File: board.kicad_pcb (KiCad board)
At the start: 6 copper layers, 197 x 134 mm, 6 parts, among them U1 MC68060RC50, U2 XC95144XL-5TQG100C, U3 SST39VF1601C-70-4C-EKE, U4 IS61WV51216BLL-10TLI, U5 IS61WV51216BLL-10TLI, U6 SST39VF1601C-70-4C-EKE

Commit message: Latest
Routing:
- net /A8: track 173.3 -> 175.7 mm
- net /A9: track 164.5 -> 166.9 mm
- net /A7: track 178.2 -> 180.5 mm
- net /A5: track 186.5 -> 188.8 mm
- net /A6: track 171.7 -> 174.0 mm
- net /A14: track 194.9 -> 196.9 mm
- net /A3: track 165.5 -> 167.0 mm
- net /D8: track 65.1 -> 66.4 mm
- net /D11: track 59.6 -> 60.8 mm
- net /D15: track 55.5 -> 56.7 mm
- net /D10: track 59.9 -> 61.1 mm
- net /D9: track 60.4 -> 61.7 mm
- net /D14: track 53.0 -> 54.3 mm
- net /A18: track 85.4 -> 86.6 mm
- net /D13: track 51.4 -> 52.6 mm
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- added copper zone on In1.Cu, net GND
- added copper zone on In4.Cu, net GND
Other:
- outline, holes or cut-outs redrawn

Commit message: First version
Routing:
- net (no net): track 42.7 -> 0.00 mm, vias 2 -> 3
- net unconnected-(U2-NC-Pad63): track 0.00 -> 23.2 mm
- net unconnected-(U2-NC-Pad67): track 0.00 -> 19.4 mm
- net GND: vias 1 -> 0
- added copper zone on In1.Cu, net (none)
- added copper zone on In4.Cu, net (none)
- removed copper zone on In1.Cu, net GND
- removed copper zone on In4.Cu, net GND
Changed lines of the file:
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@@
 		(layer "Edge.Cuts")
 	)
-	(segment
-		(start 51.677149 67.17715)
-		(end 52.5963 67.17715)
-		(width 0.2)
-		(layer "F.Cu")
-		(net "")
-	)
-	(segment
-		(start 63 75)
-		(end 69.82 75)
-		(width 0.2)
-		(layer "F.Cu")
-		(net "")
-	)
-	(segment
-		(start 56.167183 65.177149)
-		(end 57.990034 67)
-		(width 0.2)
-		(layer "F.Cu")
-		(net "")
-	)
-	(segment
-		(start 67.665 70.305)
-		(end 68.6 71.24)
-		(width 0.2)
-		(layer "F.Cu")
-		(net "")
-	)
-	(segment
-		(start 51.677149 65.177149)
-		(end 56.167183 65.177149)
-		(width 0.2)
-		(layer "F.Cu")
-		(net "")
-	)
-	(segment
-		(start 69.82 75)
-		(end 71.14 76.32)
-		(width 0.2)
-		(layer "F.Cu")
-		(net "")
-	)
-	(segment
-		(start 57.990034 67)
-		(end 60 67)
-		(width 0.2)
-		(layer "F.Cu")
-		(net "")
-	)
-	(segment
-		(start 55.5 67.5)
-		(end 63 75)
-		(width 0.2)
-		(layer "F.Cu")
-		(net "")
-	)
-	(segment
-		(start 63.305 70.305)
-		(end 67.665 70.305)
-		(width 0.2)
-		(layer "F.Cu")
-		(net "")
-	)
-	(segment
-		(start 52.5963 67.17715)
-		(end 52.91915 67.5)
-		(width 0.2)
-		(layer "F.Cu")
-		(net "")
-	)
-	(segment
-		(start 60 67)
-		(end 63.305 70.305)
-		(width 0.2)
-		(layer "F.Cu")
-		(net "")
-	)
-	(segment
-		(start 52.91915 67.5)
-		(end 55.5 67.5)
-		(width 0.2)
-		(layer "F.Cu")
+	(via
+		(at 127.20258 53.105006)
+		(size 0.6)
+		(drill 0.3)
+		(layers "F.Cu" "B.Cu")
 		(net "")
 	)
 	(via
-		(at 127.20258 53.105006)
+		(at 132 53)
 		(size 0.6)
 		(drill 0.3)
 		(layers "F.Cu" "B.Cu")
+		(free yes)
 		(net "")
 	)
@@
 	)
 	(segment
+		(start 51.677149 67.17715)
+		(end 52.5963 67.17715)
+		(width 0.2)
+		(layer "F.Cu")
+		(net "unconnected-(U2-NC-Pad63)")
+	)
+	(segment
+		(start 63 75)
+		(end 69.82 75)
+		(width 0.2)
+		(layer "F.Cu")
+		(net "unconnected-(U2-NC-Pad63)")
+	)
+	(segment
+		(start 69.82 75)
+		(end 71.14 76.32)
+		(width 0.2)
+		(layer "F.Cu")
+		(net "unconnected-(U2-NC-Pad63)")
+	)
+	(segment
+		(start 55.5 67.5)
+		(end 63 75)
+		(width 0.2)
+		(layer "F.Cu")
+		(net "unconnected-(U2-NC-Pad63)")
+	)
+	(segment
+		(start 52.5963 67.17715)
+		(end 52.91915 67.5)
+		(width 0.2)
+		(layer "F.Cu")
+		(net "unconnected-(U2-NC-Pad63)")
+	)
+	(segment
+		(start 52.91915 67.5)
+		(end 55.5 67.5)
+		(width 0.2)
+		(layer "F.Cu")
+		(net "unconnected-(U2-NC-Pad63)")
+	)
+	(segment
+		(start 56.167183 65.177149)
+		(end 57.990034 67)
+		(width 0.2)
+		(layer "F.Cu")
+		(net "unconnected-(U2-NC-Pad67)")
+	)
+	(segment
+		(start 67.665 70.305)
+		(end 68.6 71.24)
+		(width 0.2)
+		(layer "F.Cu")
+		(net "unconnected-(U2-NC-Pad67)")
+	)
+	(segment
+		(start 51.677149 65.177149)
+		(end 56.167183 65.177149)
+		(width 0.2)
+		(layer "F.Cu")
+		(net "unconnected-(U2-NC-Pad67)")
+	)
+	(segment
+		(start 57.990034 67)
+		(end 60 67)
+		(width 0.2)
+		(layer "F.Cu")
+		(net "unconnected-(U2-NC-Pad67)")
+	)
+	(segment
+		(start 63.305 70.305)
+		(end 67.665 70.305)
+		(width 0.2)
+		(layer "F.Cu")
+		(net "unconnected-(U2-NC-Pad67)")
+	)
+	(segment
+		(start 60 67)
+		(end 63.305 70.305)
+		(width 0.2)
+		(layer "F.Cu")
+		(net "unconnected-(U2-NC-Pad67)")
+	)
+	(segment
 		(start 171.065686 99.458054)
 		(end 170.996948 99.389316)
@@
 		(net "/A13")
 	)
-	(via
-		(at 132 53)
-		(size 0.6)
-		(drill 0.3)
-		(layers "F.Cu" "B.Cu")
-		(free yes)
-		(net "GND")
-	)
 	(zone
-		(net "GND")
 		(layer "In1.Cu")
 		(hatch edge 0.5)
@@
 	)
 	(zone
-		(net "GND")
 		(layer "In4.Cu")
 		(hatch edge 0.5)

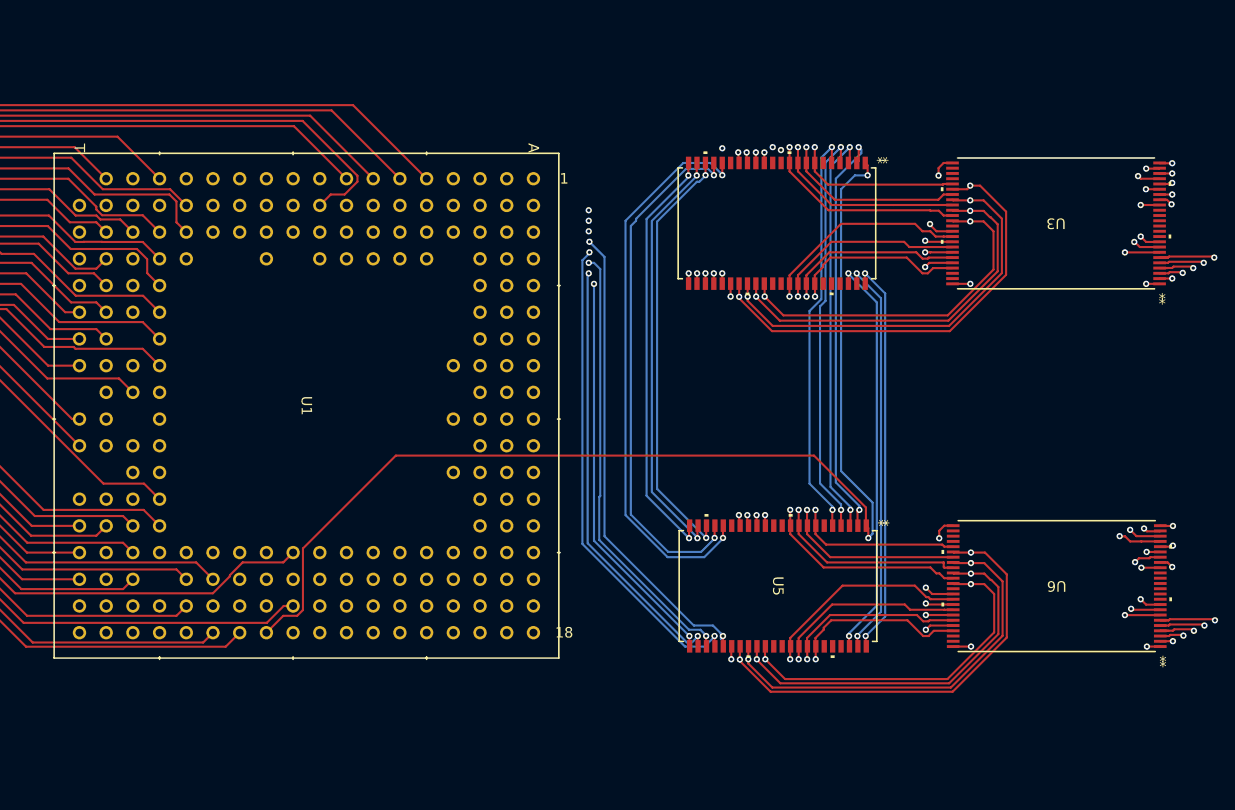
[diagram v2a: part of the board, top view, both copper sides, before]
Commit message: Power planes added
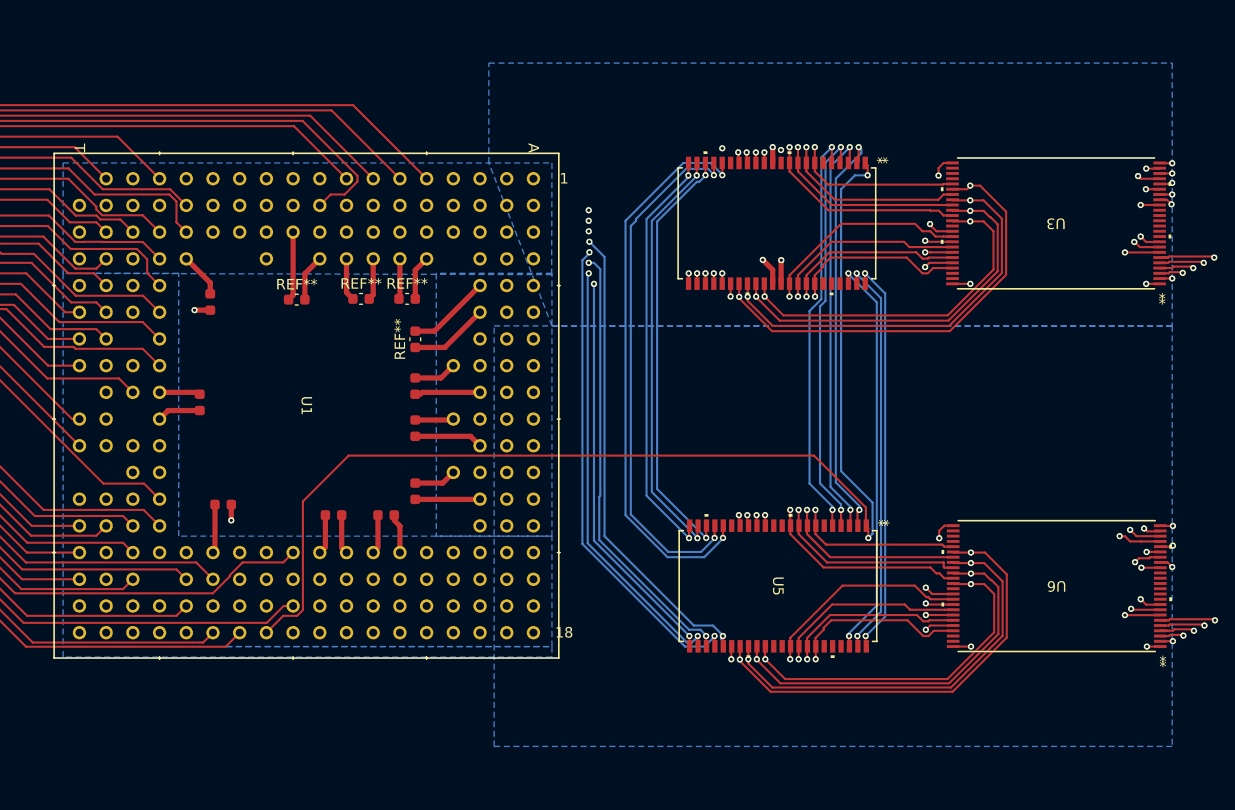
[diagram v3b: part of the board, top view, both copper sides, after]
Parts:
- added ?: , , F.Cu at (91.0, 88.0)
- added ?: , , F.Cu at (78.5, 67.0)
- added ?: , , F.Cu at (78.5, 68.5)
- added ?: , , F.Cu at (98.0, 85.0)
- added ?: , , F.Cu at (79.0, 87.0)
- added ?: , , F.Cu at (98.0, 80.5)
- added ?: , , F.Cu at (80.5, 87.0)
- added ?: , , F.Cu at (96.0, 88.0)
- added ?: , , F.Cu at (98.0, 75.0)
- added ?: , , F.Cu at (98.0, 79.0)
- added ?: , , F.Cu at (89.5, 88.0)
- added ?: , , F.Cu at (98.0, 76.5)
- added ?: , , F.Cu at (94.5, 88.0)
- added ?: , , F.Cu at (98.0, 86.5)
- added ?: , , F.Cu at (77.5, 76.5)
- added ?: , , F.Cu at (77.5, 78.0)
- added REF**: C_0603_1608Metric, Capacitor_SMD:C_0603_1608Metric, F.Cu at (98.0, 71.3)
- added REF**: C_0603_1608Metric, Capacitor_SMD:C_0603_1608Metric, F.Cu at (86.7, 67.5)
- added REF**: C_0603_1608Metric, Capacitor_SMD:C_0603_1608Metric, F.Cu at (92.8, 67.4)
- added REF**: C_0603_1608Metric, Capacitor_SMD:C_0603_1608Metric, F.Cu at (97.2, 67.4)
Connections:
- net Net-(U1C-*CLA) renamed /U1C-CLA
- net Net-(U1C-*TA) renamed /U1C-TA
- net Net-(U1C-*TIP) renamed /U1C-TIP
- net Net-(U1C-*TS) renamed /U1C-TS
- net Net-(U1C-PST0) renamed /U1C-PST0
- net Net-(U1C-PST1) renamed /U1C-PST1
- net Net-(U1C-PST2) renamed /U1C-PST2
- net Net-(U1C-PST3) renamed /U1C-PST3
- net Net-(U1C-R/*W) renamed /U1C-RW
- net Net-(U1C-SIZ0) renamed /U1C-SIZ0
- net Net-(U1C-SIZ1) renamed /U1C-SIZ1
- net Net-(U1C-TM0) renamed /U1C-TM0
- net Net-(U1C-TM1) renamed /U1C-TM1
- net Net-(U1C-TM2) renamed /U1C-TM2
- U1 pad B10: unconnected-(U1B-EVSS-PadB10) -> /GND
- U1 pad B13: unconnected-(U1B-EVSS-PadB13) -> /GND
- U1 pad B14: unconnected-(U1B-EVDD-PadB14) -> /VCC
- U1 pad B15: unconnected-(U1B-EVSS-PadB15) -> /GND
- U1 pad B17: unconnected-(U1B-EVSS-PadB17) -> /GND
- U1 pad B2: unconnected-(U1A-EVSS-PadB2) -> /GND
- U1 pad B4: unconnected-(U1A-EVSS-PadB4) -> /GND
- U1 pad B5: unconnected-(U1A-EVDD-PadB5) -> /VCC
- U1 pad B6: unconnected-(U1A-EVSS-PadB6) -> /GND
- U1 pad B8: unconnected-(U1A-EVSS-PadB8) -> /GND
- U1 pad B9: unconnected-(U1A-EVDD-PadB9) -> /VCC
- U1 pad C10: unconnected-(U1B-IVDD-PadC10) -> /VCC
- U1 pad C11: unconnected-(U1B-IVSS-PadC11) -> /GND
- U1 pad C12: unconnected-(U1B-IVDD-PadC12) -> /VCC
- U1 pad C13: unconnected-(U1B-IVSS-PadC13) -> /GND
- U1 pad C14: unconnected-(U1B-IVDD-PadC14) -> /VCC
- U1 pad C17: unconnected-(U1B-EVDD-PadC17) -> /VCC
- U1 pad C2: unconnected-(U1A-EVDD-PadC2) -> /VCC
- U1 pad C5: unconnected-(U1A-IVDD-PadC5) -> /VCC
- U1 pad C6: unconnected-(U1A-IVSS-PadC6) -> /GND
- U1 pad C7: unconnected-(U1A-IVSS-PadC7) -> /GND
- U1 pad C8: unconnected-(U1A-IVDD-PadC8) -> /VCC
- U1 pad C9: unconnected-(U1A-IVSS-PadC9) -> /GND
- U1 pad D10: unconnected-(U1B-EVDD-PadD10) -> /VCC
- U1 pad D12: unconnected-(U1B-EVDD-PadD12) -> /VCC
- U1 pad D15: unconnected-(U1B-EVDD-PadD15) -> /VCC
- U1 pad D17: unconnected-(U1B-EVSS-PadD17) -> /GND
- U1 pad D2: unconnected-(U1A-EVSS-PadD2) -> /GND
- U1 pad D8: unconnected-(U1A-EVDD-PadD8) -> /VCC
- U1 pad E15: unconnected-(U1B-IVDD-PadE15) -> /VCC
- U1 pad E4: unconnected-(U1A-EVDD-PadE4) -> /VCC
- U1 pad F15: unconnected-(U1C-IVSS-PadF15) -> /GND
- U1 pad F17: unconnected-(U1C-EVSS-PadF17) -> /GND
- U1 pad F2: unconnected-(U1A-EVSS-PadF2) -> /GND
- U1 pad F4: unconnected-(U1A-EVSS-PadF4) -> /GND
- U1 pad G15: unconnected-(U1C-EVDD-PadG15) -> /VCC
- U1 pad G17: unconnected-(U1C-EVDD-PadG17) -> /VCC
- U1 pad G2: unconnected-(U1A-EVDD-PadG2) -> /VCC
- U1 pad G4: unconnected-(U1A-EVDD-PadG4) -> /VCC
- U1 pad H15: unconnected-(U1C-IVSS-PadH15) -> /GND
- U1 pad H16: unconnected-(U1C-IVDD-PadH16) -> /VCC
- U1 pad H17: unconnected-(U1C-EVSS-PadH17) -> /GND
- U1 pad H2: unconnected-(U1A-EVSS-PadH2) -> /GND
- U1 pad H3: unconnected-(U1A-IVDD-PadH3) -> /VCC
- U1 pad H4: unconnected-(U1A-IVSS-PadH4) -> /GND
- U1 pad J15: unconnected-(U1C-EVDD-PadJ15) -> /VCC
- U1 pad J16: unconnected-(U1C-IVDD-PadJ16) -> /VCC
- U1 pad J3: unconnected-(U1A-IVDD-PadJ3) -> /VCC
- U1 pad J4: unconnected-(U1A-EVDD-PadJ4) -> /VCC
- U1 pad K16: unconnected-(U1C-IVSS-PadK16) -> /GND
- U1 pad K3: unconnected-(U1A-IVSS-PadK3) -> /GND
- U1 pad L16: unconnected-(U1C-IVDD-PadL16) -> /VCC
- U1 pad L17: unconnected-(U1C-EVSS-PadL17) -> /GND
- U1 pad L2: unconnected-(U1A-EVSS-PadL2) -> /GND
- U1 pad L3: unconnected-(U1A-IVSS-PadL3) -> /GND
- U1 pad L4: unconnected-(U1A-EVDD-PadL4) -> /VCC
- U1 pad M16: unconnected-(U1C-IVSS-PadM16) -> /GND
- U1 pad M17: unconnected-(U1C-EVDD-PadM17) -> /VCC
- U1 pad M2: unconnected-(U1A-EVDD-PadM2) -> /VCC
- U1 pad M3: unconnected-(U1A-IVDD-PadM3) -> /VCC
- U1 pad N15: unconnected-(U1C-EVDD-PadN15) -> /VCC
- U1 pad N17: unconnected-(U1C-EVSS-PadN17) -> /GND
- U1 pad N2: unconnected-(U1A-EVSS-PadN2) -> /GND
- U1 pad P2: Net-(U1A-TT1) -> /U1A-TT1
- U1 pad P3: Net-(U1A-TT0) -> /U1A-TT0
- U1 pad P4: unconnected-(U1A-EVDD-PadP4) -> /VCC
- U1 pad Q1: Net-(U1A-UPA1) -> /U1A-UPA1
- U1 pad Q10: unconnected-(U1C-EVDD-PadQ10) -> /VCC
- U1 pad Q12: unconnected-(U1C-*TRA-PadQ12) -> /U1C-TRA
- U1 pad Q13: Net-(U1C-PST4) -> /U1C-PST4
- U1 pad Q14: Net-(U1C-*SAS) -> /U1C-SAS
- U1 pad Q17: unconnected-(U1C-EVSS-PadQ17) -> /GND
- U1 pad Q2: unconnected-(U1B-EVSS-PadQ2) -> /GND
- U1 pad Q3: Net-(U1B-UPA0) -> /U1B-UPA0
- U1 pad Q8: Net-(U1B-*CLKEN) -> /U1B-CLKEN
- U1 pad Q9: unconnected-(U1B-EVSS-PadQ9) -> /GND
- U1 pad R1: unconnected-(U1B-*CIOUT-PadR1) -> /U1B-CIOUT
- U1 pad R11: unconnected-(U1C-IVSS-PadR11) -> /GND
- U1 pad R12: unconnected-(U1C-IVDD-PadR12) -> /VCC
- U1 pad R13: unconnected-(U1C-IVSS-PadR13) -> /GND
- U1 pad R17: unconnected-(U1C-EVDD-PadR17) -> /VCC
- U1 pad R2: unconnected-(U1B-EVDD-PadR2) -> /VCC
- U1 pad R3: Net-(U1B-*RSTO) -> /U1B-RSTO
- U1 pad R4: unconnected-(U1B-IVSS-PadR4) -> /GND
- U1 pad R5: unconnected-(U1B-IVDD-PadR5) -> /VCC
- U1 pad R6: unconnected-(U1B-IVSS-PadR6) -> /GND
- U1 pad R8: unconnected-(U1B-IVDD-PadR8) -> /VCC
- U1 pad R9: /CLK -> /U1B-CLK
- U1 pad S1: Net-(U1B-*IPEND) -> /U1B-IPEND
- U1 pad S10: unconnected-(U1C-IVSS-PadS10) -> /GND
- U1 pad S11: unconnected-(U1C-TBI-PadS11) -> /U1C-TBI
- U1 pad S13: unconnected-(U1C-*TEA-PadS13) -> /U1C-TEA
- U1 pad S15: unconnected-(U1C-EVSS-PadS15) -> /GND
- U1 pad S16: unconnected-(U1C-EVDD-PadS16) -> /VCC
- U1 pad S17: unconnected-(U1C-EVSS-PadS17) -> /GND
- U1 pad S2: unconnected-(U1B-EVSS-PadS2) -> /GND
- U1 pad S3: Net-(U1B-TDI) -> /U1B-TDI
- U1 pad S4: Net-(U1B-TCK) -> /U1B-TCK
- U1 pad S5: Net-(U1B-TMS) -> /U1B-TMS
- U1 pad S6: Net-(U1B-*MDIS) -> /U1B-MDIS
- U1 pad S7: /Net-(U1C-*SAS) -> /U1B-RSTI
- U1 pad S8: unconnected-(U1B-IVDD-PadS8) -> /VCC
- U1 pad S9: unconnected-(U1B-IVSS-PadS9) -> /GND
- U1 pad T10: unconnected-(U1C-*TCI-PadT10) -> /U1C-TCI
- U1 pad T11: Net-(U1C-*AVEC) -> /U1C-AVEC
- U1 pad T2: unconnected-(U1B-TDO-PadT2) -> /U1B-TDO
- U1 pad T3: unconnected-(U1B-*TRST-PadT3) -> /U1B-TRST
- U1 pad T6: Net-(U1B-*IPL2) -> /U1B-IPL2
- U1 pad T7: Net-(U1B-*IPL1) -> /U1B-IPL1
- U1 pad T8: Net-(U1B-*IPL0) -> /U1B-IPL0
- U2 pad 10: (no net) -> unconnected-(U2-IO-Pad10)
- U2 pad 11: (no net) -> unconnected-(U2-IO-Pad11)
- U2 pad 12: (no net) -> unconnected-(U2-IO-Pad12)
- U2 pad 13: (no net) -> unconnected-(U2-IO-Pad13)
- U2 pad 14: (no net) -> unconnected-(U2-IO-Pad14)
- U2 pad 15: (no net) -> unconnected-(U2-IO-Pad15)
- U2 pad 16: (no net) -> unconnected-(U2-IO-Pad16)
- U2 pad 17: (no net) -> unconnected-(U2-IO-Pad17)
- U2 pad 18: (no net) -> unconnected-(U2-IO-Pad18)
- U2 pad 19: (no net) -> unconnected-(U2-IO-Pad19)
- U2 pad 20: (no net) -> unconnected-(U2-IO-Pad20)
- U2 pad 24: (no net) -> unconnected-(U2-IO-Pad24)
- U2 pad 25: (no net) -> unconnected-(U2-IO-Pad25)
- U2 pad 28: (no net) -> unconnected-(U2-IO-Pad28)
- U2 pad 30: (no net) -> unconnected-(U2-IO-Pad30)
- U2 pad 32: (no net) -> unconnected-(U2-IO-Pad32)
- U2 pad 33: (no net) -> unconnected-(U2-IO-Pad33)
- U2 pad 50: /Net-(U1C-*SAS) -> /U1C-SAS
- U2 pad 52: (no net) -> unconnected-(U2-IO-Pad52)
- U2 pad 53: (no net) -> unconnected-(U2-IO-Pad53)
- U2 pad 54: (no net) -> unconnected-(U2-IO-Pad54)
- U2 pad 55: (no net) -> unconnected-(U2-IO-Pad55)
- U2 pad 56: (no net) -> unconnected-(U2-IO-Pad56)
- U2 pad 59: unconnected-(U2-NC-Pad59) -> /U1C-PST4
- U2 pad 6: (no net) -> unconnected-(U2-IO-Pad6)
- U2 pad 60: unconnected-(U2-NC-Pad60) -> /U1C-AVEC
- U2 pad 61: unconnected-(U2-NC-Pad61) -> /U1C-TCI
- U2 pad 63: unconnected-(U2-NC-Pad63) -> /U1B-CLK
- U2 pad 64: unconnected-(U2-NC-Pad64) -> /U1B-IPL0
- U2 pad 65: unconnected-(U2-NC-Pad65) -> /U1B-CLKEN
- U2 pad 66: unconnected-(U2-NC-Pad66) -> /U1B-IPL1
- U2 pad 67: unconnected-(U2-NC-Pad67) -> /U1B-RSTI
- U2 pad 68: unconnected-(U2-NC-Pad68) -> /BS3
- U2 pad 7: (no net) -> unconnected-(U2-IO-Pad7)
- U2 pad 70: unconnected-(U2-NC-Pad70) -> /U1B-IPL2
- U2 pad 71: unconnected-(U2-NC-Pad71) -> /U1B-MDIS
- U2 pad 72: unconnected-(U2-NC-Pad72) -> /BS2
- U2 pad 73: unconnected-(U2-NC-Pad73) -> /U1B-TMS
- U2 pad 74: unconnected-(U2-NC-Pad74) -> /U1B-TCK
- U2 pad 76: unconnected-(U2-NC-Pad76) -> /BS0
- U2 pad 78: unconnected-(U2-NC-Pad78) -> /BS1
- U2 pad 79: unconnected-(U2-NC-Pad79) -> /U1B-TDI
- U2 pad 8: (no net) -> unconnected-(U2-IO-Pad8)
- U2 pad 80: unconnected-(U2-NC-Pad80) -> /U1B-RSTO
- U2 pad 81: unconnected-(U2-NC-Pad81) -> /U1B-UPA0
- U2 pad 82: unconnected-(U2-NC-Pad82) -> /U1A-TT0
- U2 pad 83: unconnected-(U2-TDO-Pad83) -> /U1B-TD0
- U2 pad 85: unconnected-(U2-NC-Pad85) -> /U1A-TT1
- U2 pad 86: unconnected-(U2-NC-Pad86) -> /U1B-IPEND
- U2 pad 87: unconnected-(U2-NC-Pad87) -> /U1A-UPA1
- U2 pad 89: unconnected-(U2-NC-Pad89) -> /A18
- U2 pad 9: (no net) -> unconnected-(U2-IO-Pad9)
- U2 pad 90: unconnected-(U2-NC-Pad90) -> /A19
- U2 pad 91: unconnected-(U2-NC-Pad91) -> /A20
- U2 pad 92: unconnected-(U2-NC-Pad92) -> /A21
- U2 pad 93: unconnected-(U2-NC-Pad93) -> /A22
- U4 pad 12: unconnected-(U4-GND-Pad12) -> /GND
- U4 pad 33: unconnected-(U4-VDD-Pad33) -> /VCC
- U4 pad 34: unconnected-(U4-GND-Pad34) -> /GND
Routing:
- net /GND: track 0.00 -> 59.6 mm, vias 0 -> 4
- net /VCC: track 0.00 -> 55.3 mm, vias 0 -> 1
- net Net-(U1A-TT1): track 37.2 -> 0.00 mm
- net /U1A-TT1: track 0.00 -> 37.2 mm
- net Net-(U1A-UPA1): track 36.8 -> 0.00 mm
- net /U1A-UPA1: track 0.00 -> 36.8 mm
- net Net-(U1A-TT0): track 36.8 -> 0.00 mm
- net /U1A-TT0: track 0.00 -> 36.8 mm
- net Net-(U1B-UPA0): track 31.6 -> 0.00 mm
- net /U1B-UPA0: track 0.00 -> 31.6 mm
- net Net-(U1B-*IPEND): track 30.2 -> 0.00 mm
- net /U1B-IPEND: track 0.00 -> 30.2 mm
- net Net-(U1C-*SAS): track 29.5 -> 0.00 mm
- net /U1C-SAS: track 0.00 -> 29.5 mm
- net Net-(U1C-PST4): track 29.2 -> 0.00 mm
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- added copper zone on In1.Cu, net /GND
- added copper zone on In4.Cu, net /GND
- added copper zone on B.Cu, net /VCC
- removed copper zone on In1.Cu, net (none)
- removed copper zone on In4.Cu, net (none)

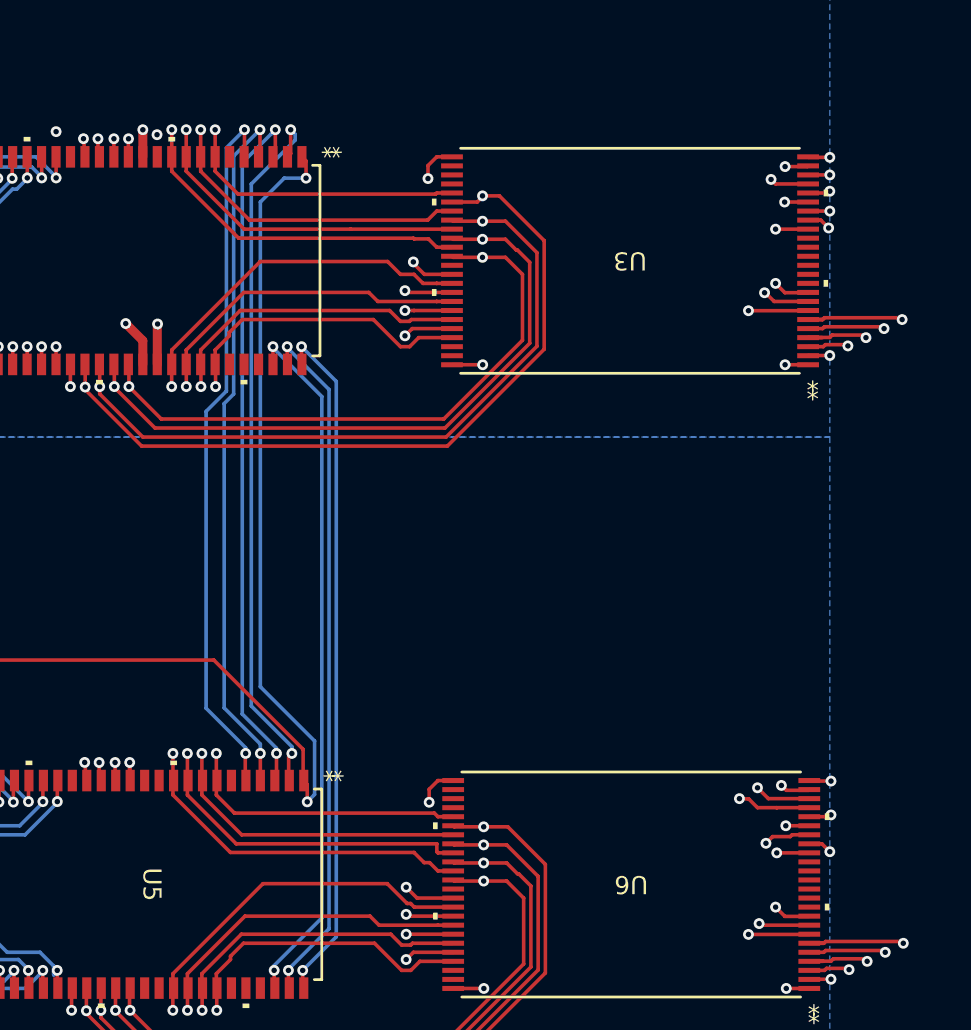
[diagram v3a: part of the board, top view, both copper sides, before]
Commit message: Started to remove via walls
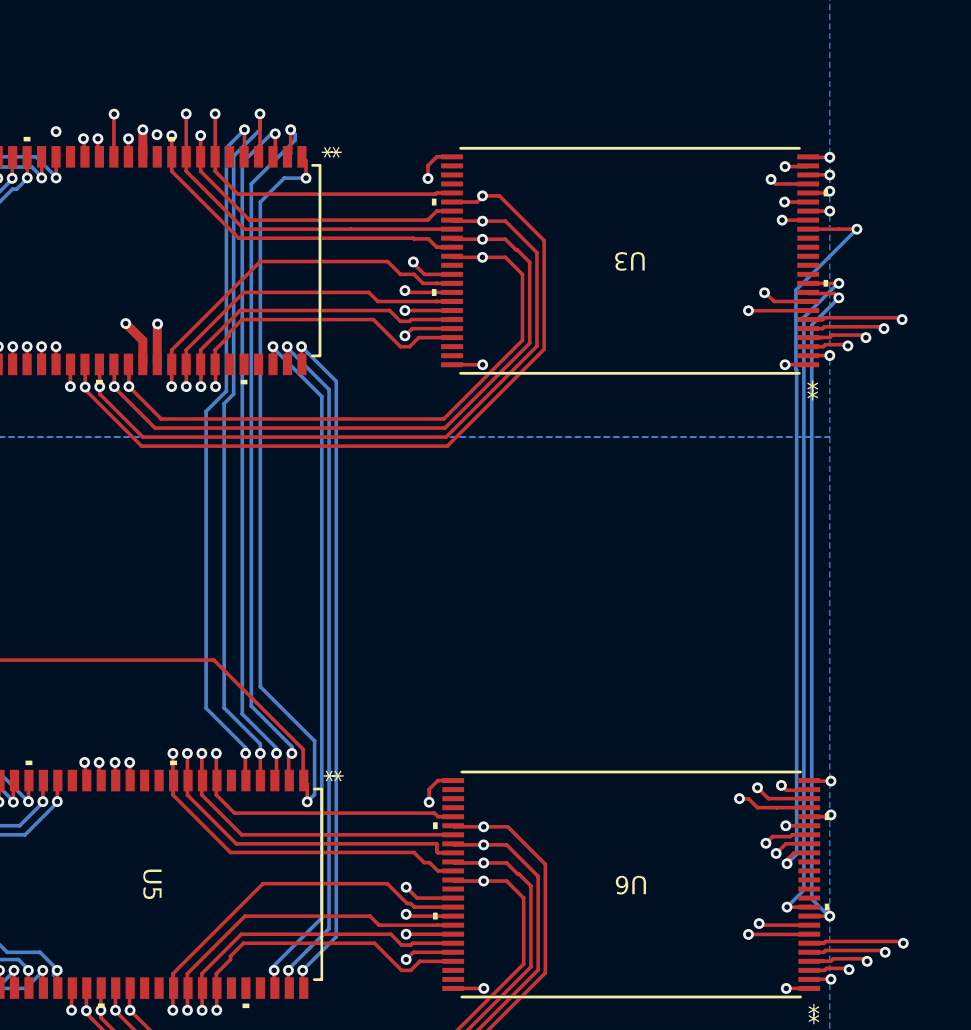
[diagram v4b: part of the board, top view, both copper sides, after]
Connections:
- U3 pad 10: unconnected-(U3-NC-Pad10) -> /A20
- U6 pad 10: unconnected-(U6-NC-Pad10) -> /A20
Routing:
- net /A19: track 68.1 -> 201.1 mm
- net /A20: track 61.7 -> 189.4 mm, vias 0 -> 2
- net /A18: track 86.6 -> 189.4 mm
- net /A17: track 180.8 -> 169.9 mm
- net /A3: track 167.0 -> 168.7 mm
- net /D5: track 52.3 -> 54.0 mm
- net /D0: track 55.6 -> 56.7 mm
- net /D1: track 53.6 -> 54.7 mm
- net /A10: track 223.4 -> 224.3 mm
- net /D2: track 57.2 -> 58.1 mm
- net /A11: track 212.4 -> 213.3 mm
- net /D3: track 48.3 -> 49.1 mm
- net /A12: track 211.4 -> 212.0 mm
- net /D4: track 50.2 -> 50.8 mm
